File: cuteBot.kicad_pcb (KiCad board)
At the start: 2 copper layers, 69 parts, among them P1 USB_A, P2 BAT+, P3 BAT-, P4 MOTOR_A, P5 MOTOR_B, P6 CONN_02X03, Q1 S8050, SW1 SW_SPDT, SW2 SW_Push, SW3 SW_Push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

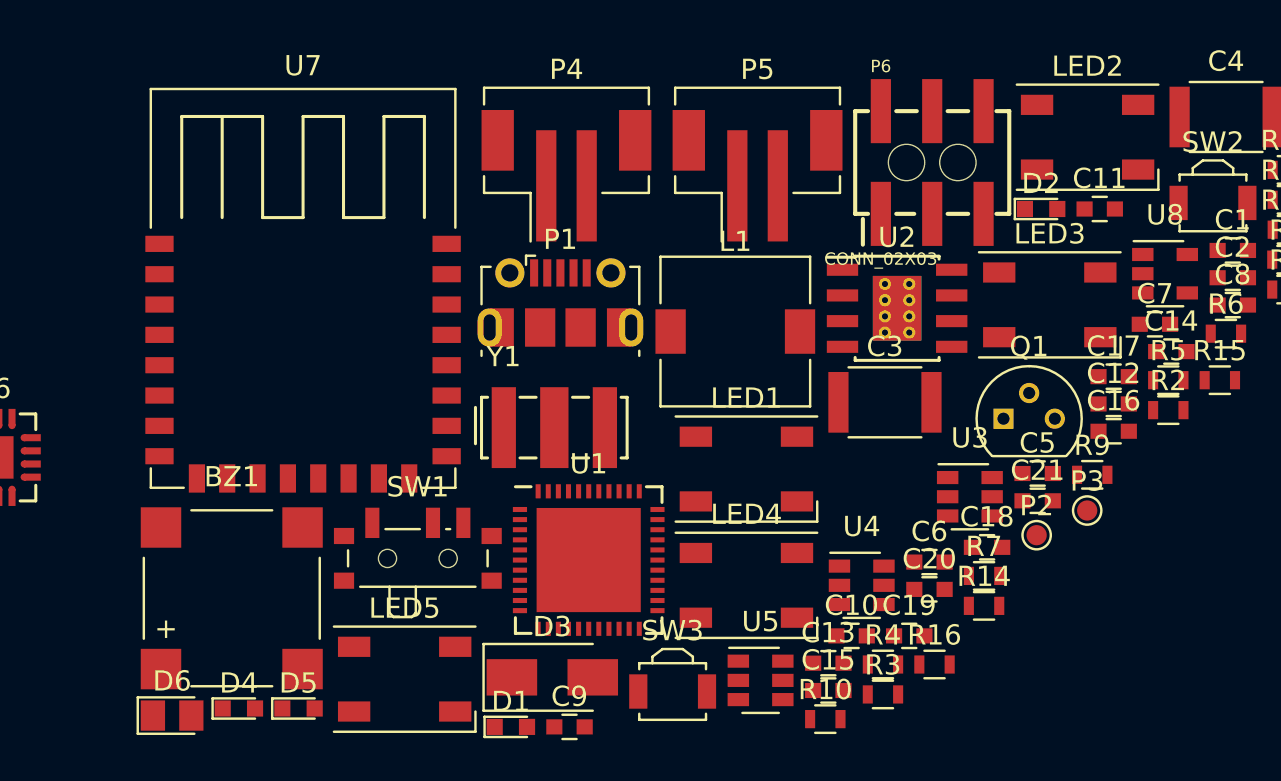
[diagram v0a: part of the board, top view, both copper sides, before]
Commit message: Footprints correctos
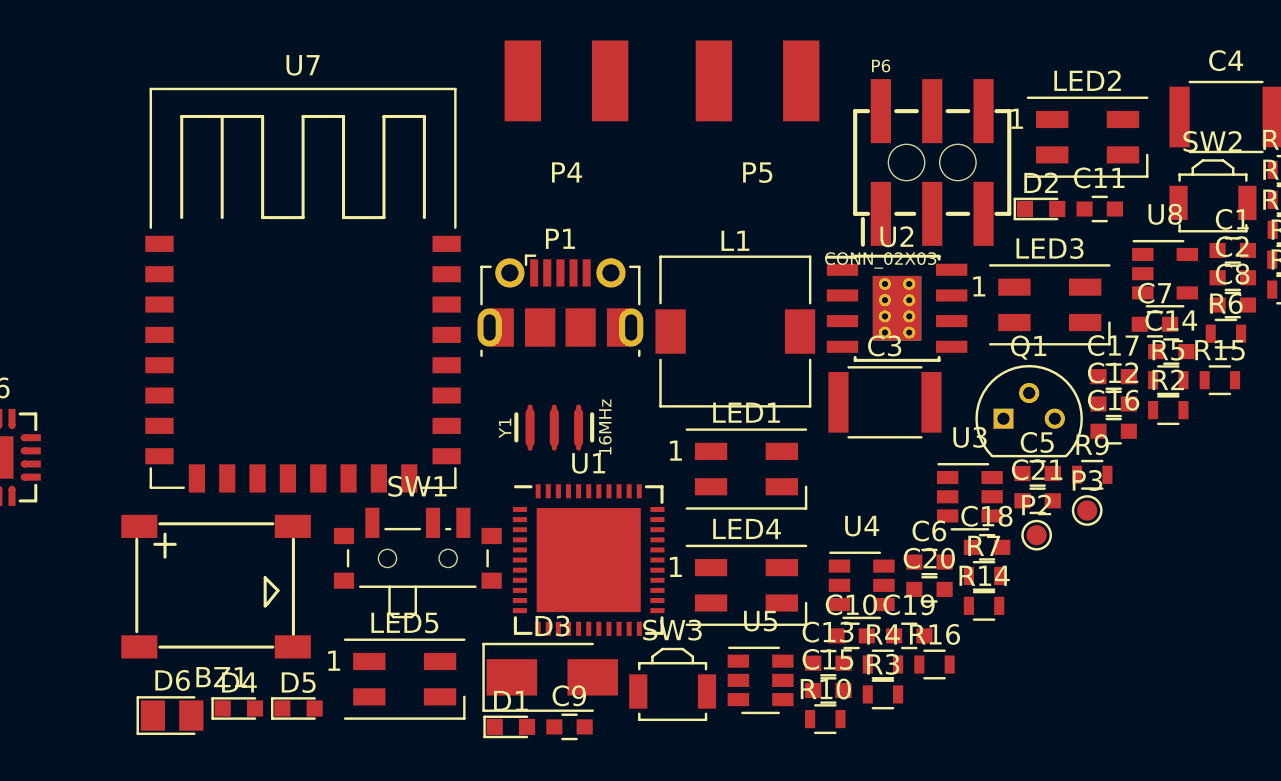
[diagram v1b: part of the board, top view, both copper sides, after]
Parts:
- BZ1: footprint Buzzers_Beepers:PUIAudio_SMT_0825_S_4_R -> frizzy_switches:Buzzer-7.5x7.5mm
- LED1, LED2, LED3, LED4, LED5: footprint LEDs:LED_WS2812B-PLCC4 -> LED:LED_SK6812MINI_PLCC4_3.5x3.5mm_P1.75mm
- P4, P5: footprint Connectors_JST:JST_PH_B2B-PH-SM4-TB_02x2.00mm_Straight -> frizzy_switches:SMD_2pin_Solderpad
- Y1: footprint Crystals:Resonator_7.2x3mm -> Clocks:RESONATOR-SMD-3.2X1.3

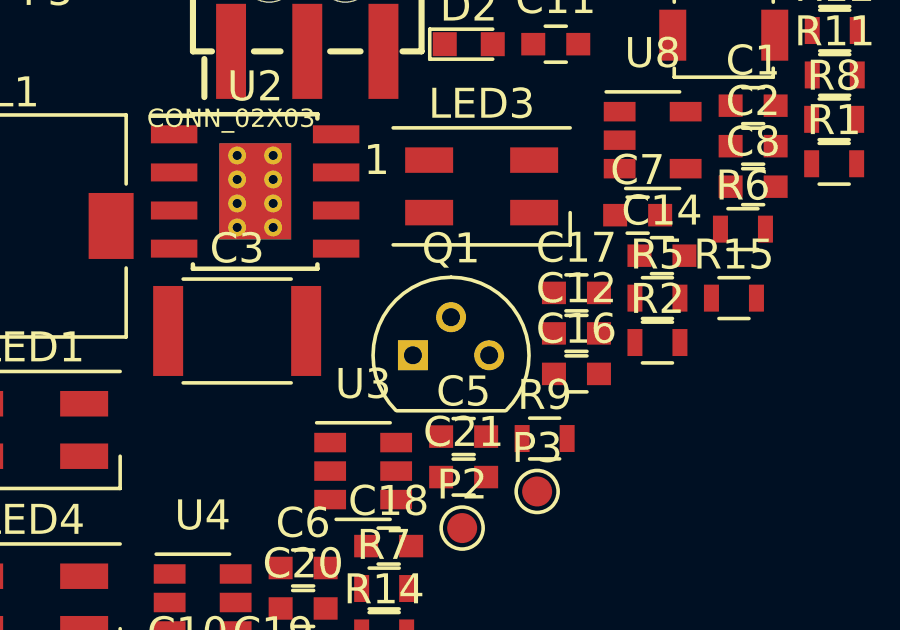
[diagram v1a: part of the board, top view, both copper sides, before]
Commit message: Error en el S8050 subsanado
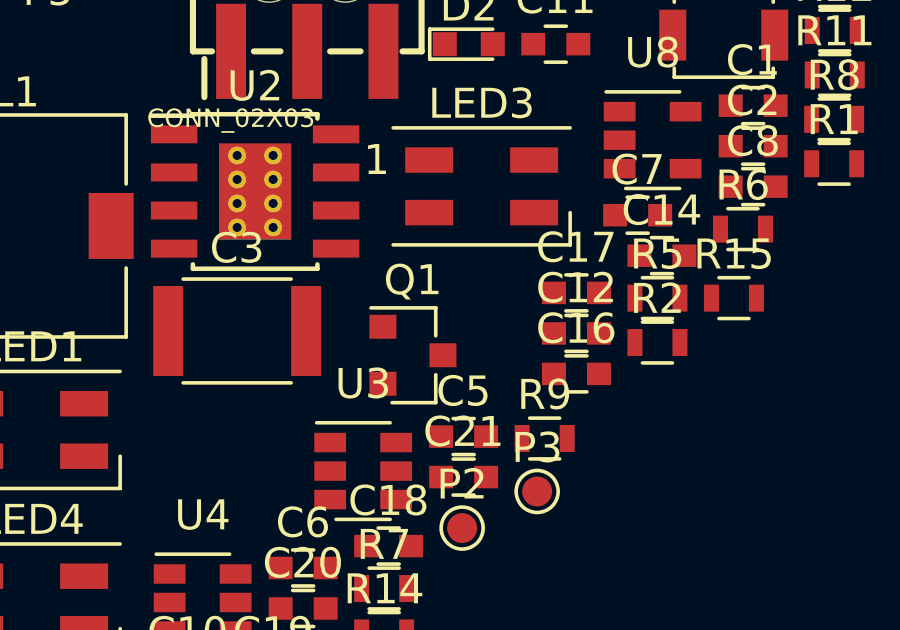
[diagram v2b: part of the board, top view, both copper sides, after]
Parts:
- Q1: footprint TO_SOT_Packages_THT:TO-92_Molded_Narrow -> TO_SOT_Packages_SMD:SOT-23
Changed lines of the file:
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@@
       (solder_mask_margin 0.1016))
-  )
-  (module TO_SOT_Packages_THT:TO-92_Molded_Narrow (layer F.Cu)
-    (at 161.680001 95.535001)
-    (descr "TO-92 leads molded, narrow, drill 0.6mm (see NXP sot054_po.pdf)")
-    (tags "to-92 sc-43 sc-43a sot54 PA33 transistor")
-    (fp_text reference Q1 (at 1.27 -3.56) (layer F.SilkS)
-      (effects (font (size 1 1) (thickness 0.15)))
-    )
-    (fp_text value S8050 (at 1.27 2.79) (layer F.Fab)
-      (effects (font (size 1 1) (thickness 0.15)))
-    )
-    (fp_text user %R (at 1.27 -3.56) (layer F.Fab)
-      (effects (font (size 1 1) (thickness 0.15)))
-    )
-    (fp_line (start -0.53 1.85) (end 3.07 1.85) (layer F.SilkS) (width 0.12))
-    (fp_line (start -0.5 1.75) (end 3 1.75) (layer F.Fab) (width 0.1))
-    (fp_line (start -1.46 -2.73) (end 4 -2.73) (layer F.CrtYd) (width 0.05))
-    (fp_line (start -1.46 -2.73) (end -1.46 2.01) (layer F.CrtYd) (width 0.05))
-    (fp_line (start 4 2.01) (end 4 -2.73) (layer F.CrtYd) (width 0.05))
-    (fp_line (start 4 2.01) (end -1.46 2.01) (layer F.CrtYd) (width 0.05))
-    (fp_arc (start 1.27 0) (end 1.27 -2.48) (angle 135) (layer F.Fab) (width 0.1))
-    (fp_arc (start 1.27 0) (end 1.27 -2.6) (angle -135) (layer F.SilkS) (width 0.12))
-    (fp_arc (start 1.27 0) (end 1.27 -2.48) (angle -135) (layer F.Fab) (width 0.1))
-    (fp_arc (start 1.27 0) (end 1.27 -2.6) (angle 135) (layer F.SilkS) (width 0.12))
-    (pad 2 thru_hole circle (at 1.27 -1.27 90) (size 1 1) (drill 0.6) (layers *.Cu *.Mask)
-      (net 38 "Net-(Q1-Pad2)"))
-    (pad 3 thru_hole circle (at 2.54 0 90) (size 1 1) (drill 0.6) (layers *.Cu *.Mask)
-      (net 1 "Net-(BZ1-Pad2)"))
-    (pad 1 thru_hole rect (at 0 0 90) (size 1 1) (drill 0.6) (layers *.Cu *.Mask)
-      (net 4 GND))
-    (model ${KISYS3DMOD}/TO_SOT_Packages_THT.3dshapes/TO-92_Molded_Narrow.wrl
-      (offset (xyz 1.269999980926514 0 0))
-      (scale (xyz 1 1 1))
-      (rotate (xyz 0 0 -90))
-    )
   )
   (module Resistors_SMD:R_0603 (layer F.Cu)
@@
       (solder_mask_margin 0.1016))
   )
+  (module TO_SOT_Packages_SMD:SOT-23 (layer F.Cu)
+    (at 161.680001 95.535001)
+    (descr "SOT-23, Standard")
+    (tags SOT-23)
+    (attr smd)
+    (fp_text reference Q1 (at 0 -2.5) (layer F.SilkS)
+      (effects (font (size 1 1) (thickness 0.15)))
+    )
+    (fp_text value S8050 (at 0 2.5) (layer F.Fab)
+      (effects (font (size 1 1) (thickness 0.15)))
+    )
+    (fp_text user %R (at 0 0 90) (layer F.Fab)
+      (effects (font (size 0.5 0.5) (thickness 0.075)))
+    )
+    (fp_line (start -0.7 -0.95) (end -0.7 1.5) (layer F.Fab) (width 0.1))
+    (fp_line (start -0.15 -1.52) (end 0.7 -1.52) (layer F.Fab) (width 0.1))
+    (fp_line (start -0.7 -0.95) (end -0.15 -1.52) (layer F.Fab) (width 0.1))
+    (fp_line (start 0.7 -1.52) (end 0.7 1.52) (layer F.Fab) (width 0.1))
+    (fp_line (start -0.7 1.52) (end 0.7 1.52) (layer F.Fab) (width 0.1))
+    (fp_line (start 0.76 1.58) (end 0.76 0.65) (layer F.SilkS) (width 0.12))
+    (fp_line (start 0.76 -1.58) (end 0.76 -0.65) (layer F.SilkS) (width 0.12))
+    (fp_line (start -1.7 -1.75) (end 1.7 -1.75) (layer F.CrtYd) (width 0.05))
+    (fp_line (start 1.7 -1.75) (end 1.7 1.75) (layer F.CrtYd) (width 0.05))
+    (fp_line (start 1.7 1.75) (end -1.7 1.75) (layer F.CrtYd) (width 0.05))
+    (fp_line (start -1.7 1.75) (end -1.7 -1.75) (layer F.CrtYd) (width 0.05))
+    (fp_line (start 0.76 -1.58) (end -1.4 -1.58) (layer F.SilkS) (width 0.12))
+    (fp_line (start 0.76 1.58) (end -0.7 1.58) (layer F.SilkS) (width 0.12))
+    (pad 1 smd rect (at -1 -0.95) (size 0.9 0.8) (layers F.Cu F.Paste F.Mask)
+      (net 4 GND))
+    (pad 2 smd rect (at -1 0.95) (size 0.9 0.8) (layers F.Cu F.Paste F.Mask)
+      (net 38 "Net-(Q1-Pad2)"))
+    (pad 3 smd rect (at 1 0) (size 0.9 0.8) (layers F.Cu F.Paste F.Mask)
+      (net 1 "Net-(BZ1-Pad2)"))
+    (model ${KISYS3DMOD}/TO_SOT_Packages_SMD.3dshapes/SOT-23.wrl
+      (at (xyz 0 0 0))
+      (scale (xyz 1 1 1))
+      (rotate (xyz 0 0 0))
+    )
+  )
 )

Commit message: Colocando los componentes
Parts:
- added REF**: MountingHole_2.2mm_M2, Mounting_Holes:MountingHole_2.2mm_M2, F.Cu at (156.2, 152.4)
- added REF**: MountingHole_2.2mm_M2, Mounting_Holes:MountingHole_2.2mm_M2, F.Cu at (121.4, 152.4)
- added REF**: MountingHole_2.2mm_M2, Mounting_Holes:MountingHole_2.2mm_M2, F.Cu at (121.4, 117.6)
- added REF**: MountingHole_2.2mm_M2, Mounting_Holes:MountingHole_2.2mm_M2, F.Cu at (156.2, 117.6)
- C10, C11, P4, P5, R11, R12, U6, U7: moved to B.Cu
- moved R12 77.2 mm to (136.9, 151.4), turned to 180 degrees
- moved R11 73.8 mm to (141.2, 151.4)
- moved SW2 67.2 mm to (122.9, 130.8), turned to 90 degrees
- moved P5 65.4 mm to (130.7, 145.5)
- moved C11 65.1 mm to (139.2, 144.3)
- moved C8 63.2 mm to (132.6, 138.4)
- moved P4 63.1 mm to (147.7, 145.5)
- moved R15 60.5 mm to (125.5, 131.8), turned to 90 degrees
- moved R8 60.3 mm to (149.1, 141.7)
- moved P6 58.8 mm to (100.8, 95.8)
- moved C7 58.6 mm to (139.7, 141.5), turned to 90 degrees
- moved U6 57.2 mm to (139.2, 147.6), turned to 90 degrees
- moved R13 54.9 mm to (153.4, 133.3), turned to 90 degrees
- moved P1 54.1 mm to (154.3, 142.7), turned to 90 degrees
- moved LED2 53.4 mm to (132.6, 123.4)
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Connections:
- U1 pad 18: Net-(U1-Pad18) -> BUZZ
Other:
- board outline added: 39.9 x 39.9 mm

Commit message: Colocando los componentes
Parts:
- moved C19 55.7 mm to (142.3, 141.4)
- moved C20 52.9 mm to (142.2, 140.0)
- moved C21 51.5 mm to (142.2, 142.7)
- moved P6 41.9 mm to (113.0, 135.9)
- moved C6 40.1 mm to (143.5, 138.4)
- moved Y1 40.1 mm to (143.5, 135.9), turned to 270 degrees
- moved C5 35.0 mm to (143.5, 133.2), turned to 180 degrees
- moved R10 7.40 mm to (125.5, 134.9), turned to 270 degrees
- moved U1 2.27 mm to (137.3, 135.5)
- moved C8 1.92 mm to (130.7, 138.6)
- moved BZ1 0.38 mm to (149.0, 131.8)
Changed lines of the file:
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@@
-(kicad_pcb (version 20171130) (host pcbnew 5.0.2-bee76a0~70~ubuntu18.04.1)
+(kicad_pcb (version 20171130) (host pcbnew "(5.0.1-3-g963ef8bb5)")
   (general
     (thickness 1.6)
@@
   )
   (module Capacitors_SMD:C_0603 (layer F.Cu)
-    (at 144.272 98.245001)
+    (at 143.498 133.223 180)
     (descr "Capacitor SMD 0603, reflow soldering, AVX (see smccp.pdf)")
     (tags "capacitor 0603")
     (attr smd)
-    (fp_text reference C5 (at 0 -1.5) (layer F.SilkS)
+    (fp_text reference C5 (at 0 -1.5 180) (layer F.SilkS)
       (effects (font (size 1 1) (thickness 0.15)))
     )
-    (fp_text value 22pF (at 0 1.5) (layer F.Fab)
+    (fp_text value 22pF (at 0 1.5 180) (layer F.Fab)
       (effects (font (size 1 1) (thickness 0.15)))
     )
@@
     (fp_line (start 0.8 0.4) (end -0.8 0.4) (layer F.Fab) (width 0.1))
     (fp_line (start -0.8 0.4) (end -0.8 -0.4) (layer F.Fab) (width 0.1))
-    (fp_text user %R (at 0 0) (layer F.Fab)
+    (fp_text user %R (at 0 0 180) (layer F.Fab)
       (effects (font (size 0.3 0.3) (thickness 0.075)))
     )
-    (pad 2 smd rect (at 0.75 0) (size 0.8 0.75) (layers F.Cu F.Paste F.Mask)
+    (pad 2 smd rect (at 0.75 0 180) (size 0.8 0.75) (layers F.Cu F.Paste F.Mask)
       (net 4 GND))
-    (pad 1 smd rect (at -0.75 0) (size 0.8 0.75) (layers F.Cu F.Paste F.Mask)
+    (pad 1 smd rect (at -0.75 0 180) (size 0.8 0.75) (layers F.Cu F.Paste F.Mask)
       (net 9 "Net-(C5-Pad1)"))
     (model Capacitors_SMD.3dshapes/C_0603.wrl
@@
   )
   (module Capacitors_SMD:C_0603 (layer F.Cu)
-    (at 138.938 98.552)
+    (at 143.51 138.43)
     (descr "Capacitor SMD 0603, reflow soldering, AVX (see smccp.pdf)")
     (tags "capacitor 0603")
@@
   )
   (module Capacitors_SMD:C_0603 (layer F.Cu)
-    (at 132.588 138.43)
+    (at 130.671 138.557)
     (descr "Capacitor SMD 0603, reflow soldering, AVX (see smccp.pdf)")
     (tags "capacitor 0603")
@@
   )
   (module Capacitors_SMD:C_0603 (layer F.Cu)
-    (at 191.504 115.316)
+    (at 142.252 141.351)
     (descr "Capacitor SMD 0603, reflow soldering, AVX (see smccp.pdf)")
     (tags "capacitor 0603")
@@
   )
   (module Capacitors_SMD:C_0603 (layer F.Cu)
-    (at 191.516 120.65)
+    (at 142.24 139.954)
     (descr "Capacitor SMD 0603, reflow soldering, AVX (see smccp.pdf)")
     (tags "capacitor 0603")
@@
   )
   (module Capacitors_SMD:C_0603 (layer F.Cu)
-    (at 191.528 127.762)
+    (at 142.24 142.748)
     (descr "Capacitor SMD 0603, reflow soldering, AVX (see smccp.pdf)")
     (tags "capacitor 0603")
@@
   )
   (module Connectors:2X3_SMT_POSTS (layer F.Cu)
-    (at 100.838 95.758)
+    (at 113.03 135.89)
     (descr "SURFACE MOUNT - 2X3 MALE HEADER WITH KEYING POSTS")
     (tags "SURFACE MOUNT - 2X3 MALE HEADER WITH KEYING POSTS")
@@
   )
   (module Resistors_SMD:R_0603 (layer F.Cu)
-    (at 132.588 136.906)
+    (at 125.476 134.862 270)
     (descr "Resistor SMD 0603, reflow soldering, Vishay (see dcrcw.pdf)")
     (tags "resistor 0603")
     (attr smd)
-    (fp_text reference R10 (at 0 -1.45) (layer F.SilkS)
+    (fp_text reference R10 (at 0 -1.45 270) (layer F.SilkS)
       (effects (font (size 1 1) (thickness 0.15)))
     )
-    (fp_text value 10k (at 0 1.5) (layer F.Fab)
+    (fp_text value 10k (at 0 1.5 270) (layer F.Fab)
       (effects (font (size 1 1) (thickness 0.15)))
     )
-    (fp_text user %R (at 0 0) (layer F.Fab)
+    (fp_text user %R (at -0.508 0 270) (layer F.Fab)
       (effects (font (size 0.4 0.4) (thickness 0.075)))
     )
@@
     (fp_line (start 1.25 0.7) (end 1.25 -0.7) (layer F.CrtYd) (width 0.05))
     (fp_line (start 1.25 0.7) (end -1.25 0.7) (layer F.CrtYd) (width 0.05))
-    (pad 1 smd rect (at -0.75 0) (size 0.5 0.9) (layers F.Cu F.Paste F.Mask)
+    (pad 1 smd rect (at -0.75 0 270) (size 0.5 0.9) (layers F.Cu F.Paste F.Mask)
       (net 37 RST))
-    (pad 2 smd rect (at 0.75 0) (size 0.5 0.9) (layers F.Cu F.Paste F.Mask)
+    (pad 2 smd rect (at 0.75 0 270) (size 0.5 0.9) (layers F.Cu F.Paste F.Mask)
       (net 8 5V))
     (model ${KISYS3DMOD}/Resistors_SMD.3dshapes/R_0603.wrl
@@
   )
   (module Housings_DFN_QFN:QFN-44-1EP_7x7mm_Pitch0.5mm (layer F.Cu)
-    (at 139.56425 135.50025 90)
+    (at 137.29575 135.48275 90)
     (descr "UK Package; 44-Lead Plastic QFN (7mm x 7mm); (see Linear Technology QFN_44_05-08-1763.pdf)")
     (tags "QFN 0.5")
@@
   )
   (module frizzy_switches:Buzzer-7.5x7.5mm (layer F.Cu)
-    (at 148.59 131.826 90)
+    (at 148.971 131.826 90)
     (fp_text reference BZ1 (at -0.508 3.937 90) (layer F.SilkS)
       (effects (font (size 1 1) (thickness 0.15)))
@@
   )
   (module Clocks:RESONATOR-SMD-3.2X1.3 (layer F.Cu)
-    (at 139.470001 95.975001)
+    (at 143.51 135.89 270)
     (descr "3.2X1.3MM 3-PIN SMD RESONATOR")
     (tags "3.2X1.3MM 3-PIN SMD RESONATOR")
     (attr smd)
-    (fp_text reference Y1 (at -2.413 0 90) (layer F.SilkS)
+    (fp_text reference Y1 (at -2.413 0) (layer F.SilkS)
       (effects (font (size 0.6096 0.6096) (thickness 0.127)))
     )
-    (fp_text value 16MHz (at 2.54 0 90) (layer F.SilkS)
+    (fp_text value 16MHz (at 2.54 0) (layer F.SilkS)
       (effects (font (size 0.6096 0.6096) (thickness 0.127)))
     )
-    (fp_text user Restrict (at 0.635 0 90) (layer Dwgs.User)
+    (fp_text user Restrict (at 1.32588 0.127) (layer Dwgs.User)
       (effects (font (size 0.254 0.254) (thickness 0.0254)))
     )
-    (fp_text user Restrict (at -0.635 0 90) (layer Dwgs.User)
+    (fp_text user Restrict (at -0.635 0) (layer Dwgs.User)
       (effects (font (size 0.254 0.254) (thickness 0.0254)))
     )
@@
     (fp_line (start 0 0) (end 0 -1.016) (layer F.Cu) (width 0.254))
     (fp_line (start 0 0) (end 0 1.016) (layer F.Cu) (width 0.254))
-    (pad 1 smd oval (at -1.19888 0) (size 0.44958 1.905) (layers F.Cu F.Paste F.Mask)
+    (pad 1 smd oval (at -1.19888 0 270) (size 0.44958 1.905) (layers F.Cu F.Paste F.Mask)
       (net 9 "Net-(C5-Pad1)") (solder_mask_margin 0.1016))
-    (pad 2 smd oval (at 0 0) (size 0.44958 1.905) (layers F.Cu F.Paste F.Mask)
+    (pad 2 smd oval (at 0 0 270) (size 0.44958 1.905) (layers F.Cu F.Paste F.Mask)
       (net 10 "Net-(C6-Pad1)") (solder_mask_margin 0.1016))
-    (pad 3 smd oval (at 1.19888 0) (size 0.44958 1.905) (layers F.Cu F.Paste F.Mask)
+    (pad 3 smd oval (at 1.19888 0 270) (size 0.44958 1.905) (layers F.Cu F.Paste F.Mask)
       (solder_mask_margin 0.1016))
   )

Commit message: Enrutando
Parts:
- C1, C17, C18, C2, C3, C4, C9, D1, D2, L1, P2, P3, R1, R2, R3, R4, R5, R6, U2, U3, U4, U5, U8: moved to B.Cu
- P6: footprint Connectors:2X3_SMT_POSTS -> Connectors:2X3_SMT_POSTS_withoput_holes
- moved C18 78.3 mm to (149.6, 140.7), turned to 270 degrees
- moved C17 74.5 mm to (142.5, 134.1), turned to 180 degrees
- moved R6 74.0 mm to (142.5, 142.5)
- moved C4 72.8 mm to (147.8, 145.3)
- moved U8 72.8 mm to (142.2, 136.7)
- moved R5 70.9 mm to (138.7, 136.7)
- moved R4 69.2 mm to (132.6, 142.8), turned to 270 degrees
- moved P2 67.6 mm to (134.9, 145.8)
- moved C1 64.5 mm to (138.7, 135.1)
- moved L1 64.3 mm to (129.5, 141.2), turned to 90 degrees
- moved C3 64.3 mm to (147.8, 136.9)
- moved C2 63.6 mm to (134.9, 133.9), turned to 180 degrees
- moved R7 58.9 mm to (148.1, 145.3)
- moved U3 57.1 mm to (135.4, 136.7), turned to 180 degrees
- moved P3 55.8 mm to (127.5, 132.3)
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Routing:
- net 5V: track 0.00 -> 103.2 mm, vias 0 -> 1
- net Vusb: track 0.00 -> 28.4 mm, vias 0 -> 1
- net Net-(R2-Pad1): track 0.00 -> 27.6 mm, vias 0 -> 2
- net Net-(R3-Pad1): track 0.00 -> 23.2 mm
- net Net-(P5-Pad2): track 0.00 -> 19.3 mm, vias 0 -> 2
- net GND: track 0.00 -> 15.5 mm, vias 0 -> 1
- net Net-(P4-Pad2): track 0.00 -> 13.6 mm, vias 0 -> 2
- net Net-(U3-Pad1): track 0.00 -> 10.8 mm, vias 0 -> 1
- net RXD: track 0.00 -> 10.5 mm, vias 0 -> 1
- net Net-(C2-Pad2): track 0.00 -> 10.1 mm
- net TXD: track 0.00 -> 9.03 mm, vias 0 -> 1
- net Net-(U3-Pad3): track 0.00 -> 6.82 mm
- net Net-(R6-Pad2): track 0.00 -> 6.50 mm, vias 0 -> 1
- net Net-(BZ1-Pad2): track 0.00 -> 6.34 mm
- net Net-(C3-Pad1): track 0.00 -> 6.20 mm, vias 0 -> 1
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- added copper zone on B.Cu, net GND
- added copper zone on F.Cu, net GND
